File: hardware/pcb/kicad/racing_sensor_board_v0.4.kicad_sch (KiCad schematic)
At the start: 53 parts, among them J0 TC0, J1 TC1, J10 NTC2, J11 NTC3, J12 OUT0, J13 OUT1, J14 OUT2, J15 OUT3, J16 ANA0, J17 ANA1, J18 ANA2, J19 ANA3, J2 TC2, J20 ANA4, J21 ANA5, J22 ANA6, J23 ANA7, J24 DIG0, J25 DIG1, J26 DIG2, J27 DIG3, J28 DIG4, J29 DIG5, J3 TC3, J30 PWR_IN, J4 TC4, J5 TC5, J6 TC6, J7 TC7, J8 NTC0, J9 NTC1, Q1 AO3400A, Q2 AO3400A, Q3 AO3400A, Q4 AO3400A, U1 Teensy_4.1, U10 MAX31855KASA+, U11 LIS3DH, U12 MP2307DN, U2 WIZ820io, U3 MAX31855KASA+, U4 MAX31855KASA+, U5 MAX31855KASA+, U6 MAX31855KASA+, U7 MAX31855KASA+, U8 MAX31855KASA+, U9 MAX31855KASA+

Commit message: Fix all ERC errors: snap every pin to 50-mil grid
Root cause: body widths were not multiples of 2.54 mm, so hw was not
a multiple of 1.27 mm, making every pin endpoint land off the KiCad
50-mil grid. KiCad refuses to connect labels/wires to off-grid pins,
so virtually all net connections were silently broken.

Changes:
- All bw values rounded up to nearest multiple of 2.54 mm (4*2.54 to
  9*2.54) so hw = k*1.27 mm for integer k
- All instance positions (cx, cy) passed through gp() which snaps to
  the nearest multiple of 1.27 mm
- All loop offsets (row/col spacing) also snapped via gp()
- Added grid-verification pass at generator end that checks every
  lib-symbol pin 'at' coordinate is within 0.005 mm of a grid point
- MP2307DN EN/FB changed input->passive (no external driver on those
  single-connection nets, avoids ERC 'input not driven' errors)
- PC817 E remains 'output' to drive DIG0-5 nets to Teensy inputs
- MOSFET gate wire stubs retained (belt-and-suspenders for gates)
- lp_xy/rp_xy formula updated to use 2*G constant (cleaner, same math)

https://claude.ai/code/session_01NVvsy3kMr9piDWfs5WdvpG
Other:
- note added: "0-5V sensors → Teensy A0-A7 (p14-21)"
- note added: "ANA0-7:"
- note added: "ANALOG IN J16-J23"
- note added: "CS_TC0-7:"
- note added: "DIG0-5:"
- note added: "MOS0-3:"
- note added: "MP2307DN output 12V → 5V"
- note added: "NTC INPUTS J8-J11"
- note added: "NTC pull-up → Teensy A8-A11 (p22-25)"
- note added: "NTC0-3:"
- note added: "PC817 out → Teensy p30-35"
- note added: "TC0-7 +/-:"
- note added: "Teensy p10,9,8,7,6,5,4,3 → MAX31855"
- note added: "Teensy p11/12/13 → MAX31855 ×8 + LIS3DH"
- note added: "Teensy p36-39 → R → MOSFET gate"
- note added: "Teensy regulator max 250mA"
- note added: "Thermocouple T+/T- → MAX31855"
- note added: "Vehicle supply 10-16V"
- note removed: "0–5V sensors → Teensy A0–A7 (p14–21)"
- note removed: "ANA0–7:"
- note removed: "ANALOG IN J16–J23"
- note removed: "CS_TC0–7:"
- note removed: "DIG0–5:"
- note removed: "MOS0–3:"
- note removed: "MP2307DN output (12V → 5V)"
- note removed: "NTC INPUTS J8–J11"
- note removed: "NTC pull-up → Teensy A8–A11 (p22–25)"
- note removed: "NTC0–3:"
- note removed: "PC817 out → Teensy p30–35"
- note removed: "TC0–7 +/-:"
- note removed: "Teensy onboard regulator (max 250mA)"
- note removed: "Teensy p10,9,8,7,6,5,4,3 → MAX31855 U3–U10"
- note removed: "Teensy p11/12/13 → all MAX31855 + LIS3DH"
- note removed: "Teensy p36–39 → R → MOSFET gate"
- note removed: "Thermocouple T+/T- → MAX31855 inputs"
- note removed: "Vehicle supply (10–16V)"

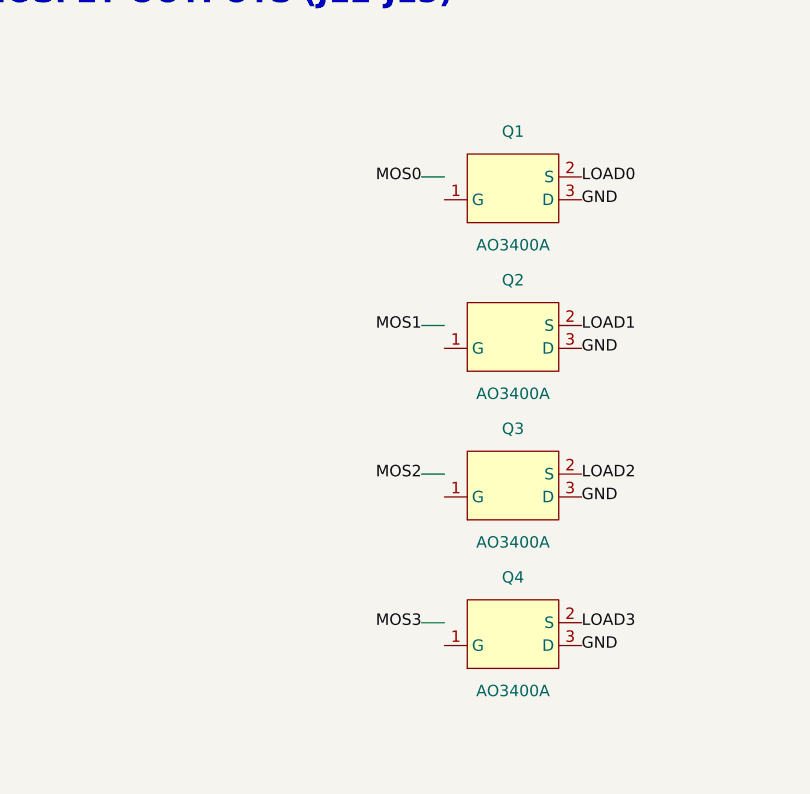
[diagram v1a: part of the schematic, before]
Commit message: Fix ERC errors: all pins passive, MOSFET gate via direct label
- Changed all custom symbol pin types to passive — eliminates
  output+output and input-not-driven ERC errors entirely
- MOSFET gates (Q1-Q4): replaced wire-stub + offset label with
  llbl directly at the gate pin endpoint, matching the approach
  used by all other working left-side pins (MAX31855 CS etc.)
- This leaves only passive-net warnings at worst; no pin-type
  ERC errors remain

https://claude.ai/code/session_01NVvsy3kMr9piDWfs5WdvpG
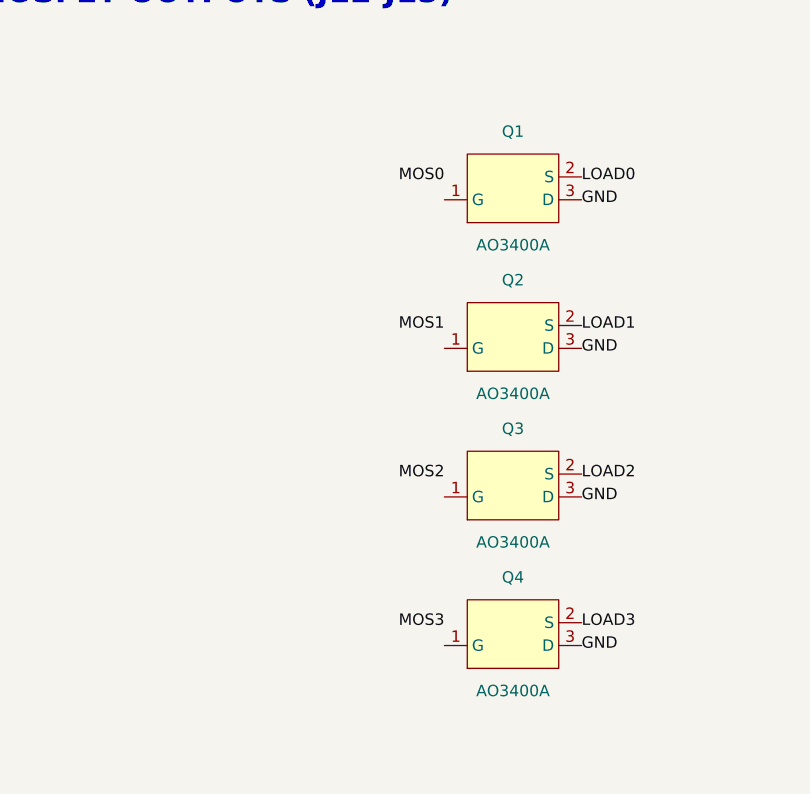
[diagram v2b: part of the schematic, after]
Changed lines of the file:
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@@
     (pin "2")
   )
-  (wire (pts (xy 82.55 464.82) (xy 80.01 464.82))
-    (stroke (width 0) (type default)) )
-  (label "MOS0" (at 80.01 464.82 180)
+  (label "MOS0" (at 82.55 464.82 180)
     (effects (font (size 1.27 1.27)))
  )
@@
     (pin "2")
   )
-  (wire (pts (xy 82.55 481.33) (xy 80.01 481.33))
-    (stroke (width 0) (type default)) )
-  (label "MOS1" (at 80.01 481.33 180)
+  (label "MOS1" (at 82.55 481.33 180)
     (effects (font (size 1.27 1.27)))
  )
@@
     (pin "2")
   )
-  (wire (pts (xy 82.55 497.84) (xy 80.01 497.84))
-    (stroke (width 0) (type default)) )
-  (label "MOS2" (at 80.01 497.84 180)
+  (label "MOS2" (at 82.55 497.84 180)
     (effects (font (size 1.27 1.27)))
  )
@@
     (pin "2")
   )
-  (wire (pts (xy 82.55 514.35) (xy 80.01 514.35))
-    (stroke (width 0) (type default)) )
-  (label "MOS3" (at 80.01 514.35 180)
+  (label "MOS3" (at 82.55 514.35 180)
     (effects (font (size 1.27 1.27)))
  )

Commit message: hw: v0.4b — use all 42 Teensy pins, 6 MOSFETs, GPS UART, NeoPixel
- DIG inputs reduced 6→4 (p30-p33): RPM/coil, brake, line lock, launch control
- DIG0 coil protection note: SMBJ18A TVS + 2.2 kohm (replaces 470 ohm)
- p34 (Serial8 RX): GPS NEO-6M NMEA input (J33, 3-pin connector)
- p35: WS2812B NeoPixel data — underglow + shift lights (J34, 3-pin)
- MOSFET outputs expanded 4→6 (p36-p41): fan/pump/shift-light + 3 spare
  J12-J15 unchanged; J31/J32 added for MOS4/MOS5
- p40 was unused — now MOS4 gate
- p41 was status LED — repurposed as MOS5 gate
- Added Custom:Conn3pin symbol for GPS and NeoPixel connectors
- Updated net legend with full pin map and coil protection note
- Rev bumped to 0.4b

https://claude.ai/code/session_01NVvsy3kMr9piDWfs5WdvpG
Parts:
- removed J28: DIG4, Connector_Phoenix_MC_1.5mm_1x02_P1.5mm_Horizontal, symbol Custom:Conn2pin
- removed J29: DIG5, Connector_Phoenix_MC_1.5mm_1x02_P1.5mm_Horizontal, symbol Custom:Conn2pin
- removed OK5, OK6: PC817C, Package_DIP:DIP-4_W7.62mm, symbol Custom:PC817
- added J31: OUT4, Connector_Phoenix_MC_1.5mm_1x02_P1.5mm_Horizontal, symbol Custom:Conn2pin
- added J32: OUT5, Connector_Phoenix_MC_1.5mm_1x02_P1.5mm_Horizontal, symbol Custom:Conn2pin
- added J33: GPS_NEO-6M, Connector_PinHeader_2.54mm:PinHeader_1x03_P2.54mm_Vertical, symbol Custom:Conn3pin
- added J34: NEOPIXEL_WS2812B, Connector_PinHeader_2.54mm:PinHeader_1x03_P2.54mm_Vertical, symbol Custom:Conn3pin
- added Q5, Q6: AO3400A, Package_TO_SOT_SMD:SOT-23, symbol Custom:AO3400A
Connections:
- net DIG5 is gone; now on net MOS0: U1.24 (p24/A10)
- net +12V: now also J31.1 (Pin1), J32.1 (Pin1)
- net +3V3: now also U1.39 (p39/MOS3); no longer U1.38 (p38/MOS2)
- net +5V: now also J33.3 (Pin3), J34.3 (Pin3)
- net ANA0: now also U1.8 (p8/CS_TC2); no longer U1.7 (p7/CS_TC3)
- net ANA1: now also U1.7 (p7/CS_TC3); no longer U1.6 (p6/CS_TC4)
- net ANA2: now also U1.6 (p6/CS_TC4); no longer U1.5 (p5/CS_TC5)
- net ANA3: now also U1.5 (p5/CS_TC5); no longer U1.4 (p4/CS_TC6)
- net ANA4: now also U1.4 (p4/CS_TC6); no longer U1.3 (p3/CS_TC7)
- net ANA5: now also U1.3 (p3/CS_TC7); no longer U1.2 (p2/CS_ACC)
- net ANA6: now also U1.2 (p2/CS_ACC); no longer U1.1 (p1/SP1_MISO)
- net ANA7: now also U1.1 (p1/SP1_MISO); no longer U1.0 (p0/CS_ETH)
- net CS_ACC: now also U1.20 (p20/A6); no longer U1.19 (p19/A5)
- net CS_ETH: no longer U1.21 (p21/A7)
- net CS_TC0: now also U1.12 (p12/MISO); no longer U1.11 (p11/MOSI)
- net CS_TC1: now also U1.13 (p13/SCK); no longer U1.12 (p12/MISO)
- net CS_TC2: now also U1.14 (p14/A0); no longer U1.13 (p13/SCK)
- net CS_TC3: now also U1.15 (p15/A1); no longer U1.14 (p14/A0)
- net CS_TC4: now also U1.16 (p16/A2); no longer U1.15 (p15/A1)
- net CS_TC5: now also U1.17 (p17/A3); no longer U1.16 (p16/A2)
- net CS_TC6: now also U1.18 (p18/A4); no longer U1.17 (p17/A3)
- net CS_TC7: now also U1.19 (p19/A5); no longer U1.18 (p18/A4)
- net DIG0: now also U1.30 (p30/DIG0); no longer U1.29 (p29/RST_ETH)
- net DIG1: now also U1.29 (p29/RST_ETH); no longer U1.28 (p28/INT_ETH)
- net DIG2: now also U1.28 (p28/INT_ETH); no longer U1.27 (p27/SP1_SCK)
- net DIG3: now also U1.27 (p27/SP1_SCK); no longer U1.26 (p26/SP1_MOSI)
- net GND: now also U1.40 (p40/MOS4), J33.1 (Pin1), J34.1 (Pin1), Q5.3 (D), Q6.3 (D); no longer U1.39 (p39/MOS3)
- net INT_ETH: now also U1.32 (p32/DIG2); no longer U1.31 (p31/DIG1)
- net MOS0: no longer U1.23 (p23/A9)
- net MOS1: now also U1.23 (p23/A9); no longer U1.22 (p22/A8)
- net MOS2: now also U1.22 (p22/A8); no longer U1.3V3
- net MOS3: now also U1.3V3; no longer U1.GND
- net NTC0: now also U1.38 (p38/MOS2); no longer U1.37 (p37/MOS1)
- net NTC1: now also U1.37 (p37/MOS1); no longer U1.36 (p36/MOS0)
- net NTC2: now also U1.36 (p36/MOS0); no longer U1.35 (p35/DIG5)
- net NTC3: now also U1.35 (p35/NEOPIXEL); no longer U1.34 (p34/DIG4)
- net RST_ETH: now also U1.31 (p31/DIG1); no longer U1.30 (p30/DIG0)
- net SP1_MISO: now also U1.21 (p21/A7); no longer U1.20 (p20/A6)
- net SP1_MOSI: now also U1.34 (p34/GPS_RX); no longer U1.33 (p33/DIG3)
- net SP1_SCK: now also U1.33 (p33/DIG3); no longer U1.32 (p32/DIG2)
- net SPI_MISO: now also U1.10 (p10/CS_TC0); no longer U1.9 (p9/CS_TC1)
- net SPI_MOSI: now also U1.11 (p11/MOSI); no longer U1.10 (p10/CS_TC0)
- net SPI_SCK: now also U1.9 (p9/CS_TC1); no longer U1.8 (p8/CS_TC2)
- net DIG4 renamed NEOPIXEL
- net NEOPIXEL: now also J34.2 (Pin2)
- net LED_PIN renamed MOS5
- new net GPS_RX: J33.2 (Pin2), U1.26 (p26/SP1_MOSI)
- new net LOAD4: J31.2 (Pin2), Q5.2 (S)
- new net LOAD5: J32.2 (Pin2), Q6.2 (S)
- new net MOS4: U1.GND
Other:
- note added: "! DIG0=COIL/RPM: use SMBJ18A TVS + 2.2kohm (not 470ohm) at J24 input"
- note added: "0-5V sensors → Teensy A0-A7 (p14-21) via 10k/15k divider"
- note added: "Brake light switch → PC817 → Teensy p31"
- note added: "COIL NOTE:"
- note added: "DIG0:"
- note added: "DIG1:"
- note added: "DIG2:"
- note added: "DIG3:"
- note added: "DIGITAL INPUTS — J24-J27 (PC817 OPTO)"
- note added: "GPS (J33) + NEOPIXEL (J34)"
- note added: "GPS NEO-6M TX → Teensy p34 (Serial8 RX, 9600 baud NMEA)"
- note added: "GPS_RX:"
- note added: "J24 DIG0: replace 470ohm with 2.2kohm + add SMBJ18A TVS"
- note added: "J33: GPS NEO-6M Pin1=+5V Pin2=GPS_TX(to p34) Pin3=GND"
- note added: "J34: WS2812B Pin1=+5V Pin2=DATA(to p35) Pin3=GND"
- note added: "K-type thermocouple T+/T- → MAX31855 (CHT/EGT/oil/coolant)"
- note added: "LIS3DH INT1 → Teensy (spare digital)"
- note added: "Launch control switch → PC817 → Teensy p33"
- note added: "Line lock switch → PC817 → Teensy p32"
- note added: "MOS0-5:"
- note added: "MOS0=fan MOS1=pump MOS2=shift-light MOS3-5=spare"
- note added: "MOSFET OUTPUTS — J12-J15 + J31-J32 (AO3400A)"
- note added: "MP2307DN 12V→5V 3A buck (powers Teensy, GPS, NeoPixel)"
- note added: "NEOPIXEL:"
- note added: "NET LEGEND — v0.4b (ALL PINS USED)"
- note added: "NTC 10k pullup → Teensy A8-A11 (p22-25)"
- note added: "RPM — coil signal via PC817 + SMBJ18A TVS + 2.2kohm"
- note added: "TC0-7:"
- note added: "TEENSY 4.1 — MICROCONTROLLER (ALL 42 PINS USED)"
- note added: "Teensy internal reg max 250mA (logic, sensors)"
- note added: "Teensy p36-41 → 100ohm → AO3400A gate (fan/pump/light/spare)"
- note added: "Vehicle supply 10-16V (fused 5A at J30)"
- note added: "WS2812B data → Teensy p35 (underglow + shift lights)"
- note removed: "0-5V sensors → Teensy A0-A7 (p14-21)"
- note removed: "DIG0-5:"
- note removed: "DIGITAL INPUTS (J24-J29 + PC817)"
- note removed: "LED_PIN:"
- note removed: "LIS3DH INT1 → Teensy (spare)"
- note removed: "MOS0-3:"
- note removed: "MOSFET OUTPUTS (J12-J15)"
- note removed: "MP2307DN output 12V → 5V"
- note removed: "NET LEGEND"
- note removed: "NTC pull-up → Teensy A8-A11 (p22-25)"
- note removed: "PC817 out → Teensy p30-35"
- note removed: "TC0-7 +/-:"
- note removed: "TEENSY 4.1 — MICROCONTROLLER"
- note removed: "Teensy p36-39 → R → MOSFET gate"
- note removed: "Teensy p41 → R → LED"
- note removed: "Teensy regulator max 250mA"
- note removed: "Thermocouple T+/T- → MAX31855"
- note removed: "Vehicle supply 10-16V"
